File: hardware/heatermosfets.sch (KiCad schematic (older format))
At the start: 39 parts, among them Q1 BUK7M33-60EX, Q2 BUK7M33-60EX, Q3 BUK7M33-60EX, U2 LT1910, U5 OPAMP, U6 LT1910, U7 OPAMP, U8 LT1910, U9 OPAMP

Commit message: Updated Andersons and layout
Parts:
- removed Conn2, Conn5, Conn8: Molex_uF_S_02, MRDT_Connectors:MOLEX_uF_S_02_Horizontal, symbol MRDT_Connectors:Molex_uF_S_02
- removed R10, R12, R13, R14, R15, R2, R3, R4, R5, R7, R8, R9: R, Resistor_SMD:R_0603_1608Metric_Pad0.98x0.95mm_HandSolder, symbol Device:R
- removed U5, U7, U9: OPAMP, Package_SO:SOIC-14_3.9x8.7mm_P1.27mm, symbol pspice:OPAMP
- added Conn3, Conn6, Conn9: Molex_uF_S_03, MRDT_Connectors:MOLEX_uF_S_03_Horizontal, symbol MRDT_Connectors:Molex_uF_S_03
- renumbered C16 to C10, C17 to C11, C18 to C12, C19 to C13, C1 to C8, C2 to C9, Conn9 to Conn10, Conn10 to Conn11, Conn3 to Conn4, Conn4 to Conn5, Conn6 to Conn7, Conn7 to Conn8, R6 to R2, R11 to R3, U2 to U4, U6 to U5, U8 to U6
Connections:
- net +3V3: now also Conn3.1, Conn6.1, Conn9.1
- net GND: now also Conn3.3, Conn6.3, Conn9.3
- net pair1_out: now also Conn3.2
- net pair2_out: now also Conn6.2
- net pair3_out: now also Conn9.2
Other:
- note added: "Temp. Sensor"
- note removed: "Thermistor"

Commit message: Finished layout?
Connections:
- net +12V renamed +12VA
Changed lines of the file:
@@
 Wire Wire Line
 	3200 1550 3200 1700
-$Comp
-L power:+12V #PWR?
-U 1 1 618FC159
-P 2550 1450
-AR Path="/618FC159" Ref="#PWR?"  Part="1"
-AR Path="/618CFEA8/618FC159" Ref="#PWR015"  Part="1"
-F 0 "#PWR015" H 2550 1300 50  0001 C CNN
-F 1 "+12V" H 2565 1623 50  0000 C CNN
-F 2 "" H 2550 1450 50  0001 C CNN
-F 3 "" H 2550 1450 50  0001 C CNN
-	1    2550 1450
-	1    0    0    -1
-$EndComp
 Wire Wire Line
 	2450 1700 3200 1700
@@
 Wire Wire Line
 	6750 1550 6750 1700
-$Comp
-L power:+12V #PWR?
-U 1 1 619075FA
-P 6100 1450
-AR Path="/619075FA" Ref="#PWR?"  Part="1"
-AR Path="/618CFEA8/619075FA" Ref="#PWR020"  Part="1"
-F 0 "#PWR020" H 6100 1300 50  0001 C CNN
-F 1 "+12V" H 6115 1623 50  0000 C CNN
-F 2 "" H 6100 1450 50  0001 C CNN
-F 3 "" H 6100 1450 50  0001 C CNN
-	1    6100 1450
-	1    0    0    -1
-$EndComp
 Wire Wire Line
 	6000 1700 6750 1700
@@
 Wire Wire Line
 	10200 1550 10200 1700
-$Comp
-L power:+12V #PWR?
-U 1 1 61917C2A
-P 9550 1450
-AR Path="/61917C2A" Ref="#PWR?"  Part="1"
-AR Path="/618CFEA8/61917C2A" Ref="#PWR025"  Part="1"
-F 0 "#PWR025" H 9550 1300 50  0001 C CNN
-F 1 "+12V" H 9565 1623 50  0000 C CNN
-F 2 "" H 9550 1450 50  0001 C CNN
-F 3 "" H 9550 1450 50  0001 C CNN
-	1    9550 1450
-	1    0    0    -1
-$EndComp
 Wire Wire Line
 	9450 1700 10200 1700
@@
 Text Notes 10950 3150 0    39   ~ 0
 Temp. Sensor
+$Comp
+L power:+12VA #PWR?
+U 1 1 6190F302
+P 2550 1450
+F 0 "#PWR?" H 2550 1300 50  0001 C CNN
+F 1 "+12VA" H 2565 1623 50  0000 C CNN
+F 2 "" H 2550 1450 50  0001 C CNN
+F 3 "" H 2550 1450 50  0001 C CNN
+	1    2550 1450
+	1    0    0    -1
+$EndComp
+$Comp
+L power:+12VA #PWR?
+U 1 1 61912CB5
+P 6100 1450
+F 0 "#PWR?" H 6100 1300 50  0001 C CNN
+F 1 "+12VA" H 6115 1623 50  0000 C CNN
+F 2 "" H 6100 1450 50  0001 C CNN
+F 3 "" H 6100 1450 50  0001 C CNN
+	1    6100 1450
+	1    0    0    -1
+$EndComp
+$Comp
+L power:+12VA #PWR?
+U 1 1 61913A07
+P 9550 1450
+F 0 "#PWR?" H 9550 1300 50  0001 C CNN
+F 1 "+12VA" H 9565 1623 50  0000 C CNN
+F 2 "" H 9550 1450 50  0001 C CNN
+F 3 "" H 9550 1450 50  0001 C CNN
+	1    9550 1450
+	1    0    0    -1
+$EndComp
 $EndSCHEMATC

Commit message: Fixed rescue library
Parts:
- U4, U5, U6: symbol hardware-rescue:LT1910-MRDT_ICs -> MRDT_ICs:LT1910
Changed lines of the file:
@@
 $EndDescr
 $Comp
-L hardware-rescue:LT1910-MRDT_ICs U?
+L MRDT_ICs:LT1910 U?
 U 1 1 618FC10F
 P 1500 1950
@@
 pair1_in
 $Comp
-L hardware-rescue:LT1910-MRDT_ICs U?
+L MRDT_ICs:LT1910 U?
 U 1 1 619075B4
 P 5050 1950
@@
 pair2_in
 $Comp
-L hardware-rescue:LT1910-MRDT_ICs U?
+L MRDT_ICs:LT1910 U?
 U 1 1 61917BE4
 P 8500 1950

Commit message: Initial Rev2 Design
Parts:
- added D3, D4, D5: LED, LED_SMD:LED_0603_1608Metric_Pad1.05x0.95mm_HandSolder, symbol Device:LED
- added R10, R11, R12: 120, Resistor_SMD:R_0603_1608Metric_Pad0.98x0.95mm_HandSolder, symbol Device:R
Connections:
- net GND: now also D3.1 (K), D4.1 (K), D5.1 (K)
- net pair1_in: now also R10.1
- net pair2_in: now also R11.1
- net pair3_in: now also R12.1
- new net: D5.2 (A), R12.2
- new net: D4.2 (A), R11.2
- new net: D3.2 (A), R10.2
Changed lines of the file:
@@
 	1900 2750 1900 2600
 Wire Wire Line
-	950  1700 1300 1700
+	850  1700 950  1700
 Text Notes 1600 1200 0    59   ~ 12
 Gate Driver
@@
 Wire Wire Line
 	3900 1000 3900 1450
-Text HLabel 950  1700 0    50   Input ~ 0
+Text HLabel 850  1700 0    50   Input ~ 0
 pair1_in
 $Comp
@@
 	5450 2750 5450 2600
 Wire Wire Line
-	4500 1700 4850 1700
+	4400 1700 4500 1700
 Text Notes 5150 1200 0    59   ~ 12
 Gate Driver
@@
 Wire Wire Line
 	7450 1000 7450 1450
-Text HLabel 4500 1700 0    50   Input ~ 0
+Text HLabel 4400 1700 0    50   Input ~ 0
 pair2_in
 $Comp
@@
 	8900 2750 8900 2600
 Wire Wire Line
-	7950 1700 8300 1700
+	7850 1700 7950 1700
 Text Notes 8600 1200 0    59   ~ 12
 Gate Driver
@@
 Wire Wire Line
 	10900 1000 10900 1450
-Text HLabel 7950 1700 0    50   Input ~ 0
+Text HLabel 7850 1700 0    50   Input ~ 0
 pair3_in
 Wire Wire Line
@@
 Temp. Sensor
 $Comp
-L power:+12VA #PWR?
+L power:+12VA #PWR015
 U 1 1 6190F302
 P 2550 1450
-F 0 "#PWR?" H 2550 1300 50  0001 C CNN
+F 0 "#PWR015" H 2550 1300 50  0001 C CNN
 F 1 "+12VA" H 2565 1623 50  0000 C CNN
 F 2 "" H 2550 1450 50  0001 C CNN
@@
 $EndComp
 $Comp
-L power:+12VA #PWR?
+L power:+12VA #PWR020
 U 1 1 61912CB5
 P 6100 1450
-F 0 "#PWR?" H 6100 1300 50  0001 C CNN
+F 0 "#PWR020" H 6100 1300 50  0001 C CNN
 F 1 "+12VA" H 6115 1623 50  0000 C CNN
 F 2 "" H 6100 1450 50  0001 C CNN
@@
 $EndComp
 $Comp
-L power:+12VA #PWR?
+L power:+12VA #PWR025
 U 1 1 61913A07
 P 9550 1450
-F 0 "#PWR?" H 9550 1300 50  0001 C CNN
+F 0 "#PWR025" H 9550 1300 50  0001 C CNN
 F 1 "+12VA" H 9565 1623 50  0000 C CNN
 F 2 "" H 9550 1450 50  0001 C CNN
@@
 	1    0    0    -1
 $EndComp
+Wire Wire Line
+	7950 1700 7950 1850
+Wire Wire Line
+	7950 1850 7800 1850
+Connection ~ 7950 1700
+Wire Wire Line
+	7950 1700 8300 1700
+Wire Wire Line
+	7800 2550 7800 2600
+Wire Wire Line
+	7800 2600 8100 2600
+Connection ~ 8100 2600
+Wire Wire Line
+	4500 1850 4350 1850
+Wire Wire Line
+	4500 1700 4500 1850
+Connection ~ 4500 1700
+Wire Wire Line
+	4500 1700 4850 1700
+Wire Wire Line
+	4350 2550 4350 2600
+Wire Wire Line
+	4350 2600 4650 2600
+Connection ~ 4650 2600
+Wire Wire Line
+	950  1700 950  1850
+Wire Wire Line
+	950  1850 800  1850
+Connection ~ 950  1700
+Wire Wire Line
+	950  1700 1300 1700
+Wire Wire Line
+	800  2550 800  2600
+Wire Wire Line
+	800  2600 1100 2600
+Connection ~ 1100 2600
+$Comp
+L Device:LED D5
+U 1 1 6228CFC5
+P 7800 2400
+F 0 "D5" V 7800 2300 50  0000 R CNN
+F 1 "LED" V 7700 2300 50  0000 R CNN
+F 2 "LED_SMD:LED_0603_1608Metric_Pad1.05x0.95mm_HandSolder" H 7800 2400 50  0001 C CNN
+F 3 "~" H 7800 2400 50  0001 C CNN
+	1    7800 2400
+	0    -1   -1   0
+$EndComp
+$Comp
+L Device:LED D4
+U 1 1 6228DEBB
+P 4350 2400
+F 0 "D4" V 4350 2300 50  0000 R CNN
+F 1 "LED" V 4250 2300 50  0000 R CNN
+F 2 "LED_SMD:LED_0603_1608Metric_Pad1.05x0.95mm_HandSolder" H 4350 2400 50  0001 C CNN
+F 3 "~" H 4350 2400 50  0001 C CNN
+	1    4350 2400
+	0    -1   -1   0
+$EndComp
+$Comp
+L Device:LED D3
+U 1 1 6228F1AF
+P 800 2400
+F 0 "D3" V 800 2300 50  0000 R CNN
+F 1 "LED" V 700 2300 50  0000 R CNN
+F 2 "LED_SMD:LED_0603_1608Metric_Pad1.05x0.95mm_HandSolder" H 800 2400 50  0001 C CNN
+F 3 "~" H 800 2400 50  0001 C CNN
+	1    800  2400
+	0    -1   -1   0
+$EndComp
+Wire Wire Line
+	800  1850 800  1900
+Wire Wire Line
+	4350 1850 4350 1900
+Wire Wire Line
+	7800 1850 7800 1900
+$Comp
+L Device:R R10
+U 1 1 623BB9D6
+P 800 2050
+F 0 "R10" H 870 2096 50  0000 L CNN
+F 1 "120" H 870 2005 50  0000 L CNN
+F 2 "Resistor_SMD:R_0603_1608Metric_Pad0.98x0.95mm_HandSolder" V 730 2050 50  0001 C CNN
+F 3 "~" H 800 2050 50  0001 C CNN
+	1    800  2050
+	1    0    0    -1
+$EndComp
+Wire Wire Line
+	800  2200 800  2250
+$Comp
+L Device:R R11
+U 1 1 623CE605
+P 4350 2050
+F 0 "R11" H 4420 2096 50  0000 L CNN
+F 1 "120" H 4420 2005 50  0000 L CNN
+F 2 "Resistor_SMD:R_0603_1608Metric_Pad0.98x0.95mm_HandSolder" V 4280 2050 50  0001 C CNN
+F 3 "~" H 4350 2050 50  0001 C CNN
+	1    4350 2050
+	1    0    0    -1
+$EndComp
+Wire Wire Line
+	4350 2200 4350 2250
+$Comp
+L Device:R R12
+U 1 1 623D346B
+P 7800 2050
+F 0 "R12" H 7870 2096 50  0000 L CNN
+F 1 "120" H 7870 2005 50  0000 L CNN
+F 2 "Resistor_SMD:R_0603_1608Metric_Pad0.98x0.95mm_HandSolder" V 7730 2050 50  0001 C CNN
+F 3 "~" H 7800 2050 50  0001 C CNN
+	1    7800 2050
+	1    0    0    -1
+$EndComp
+Wire Wire Line
+	7800 2200 7800 2250
 $EndSCHEMATC

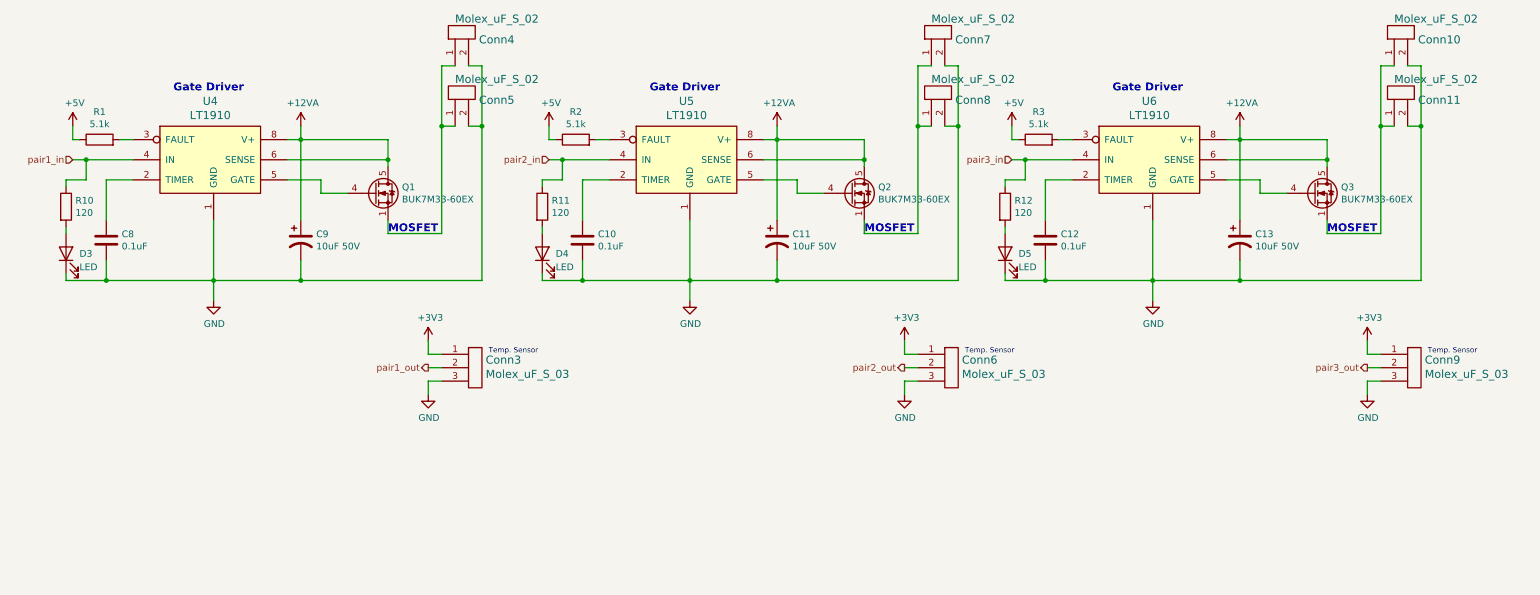
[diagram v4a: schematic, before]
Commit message: Fixed Mosfet LEDs
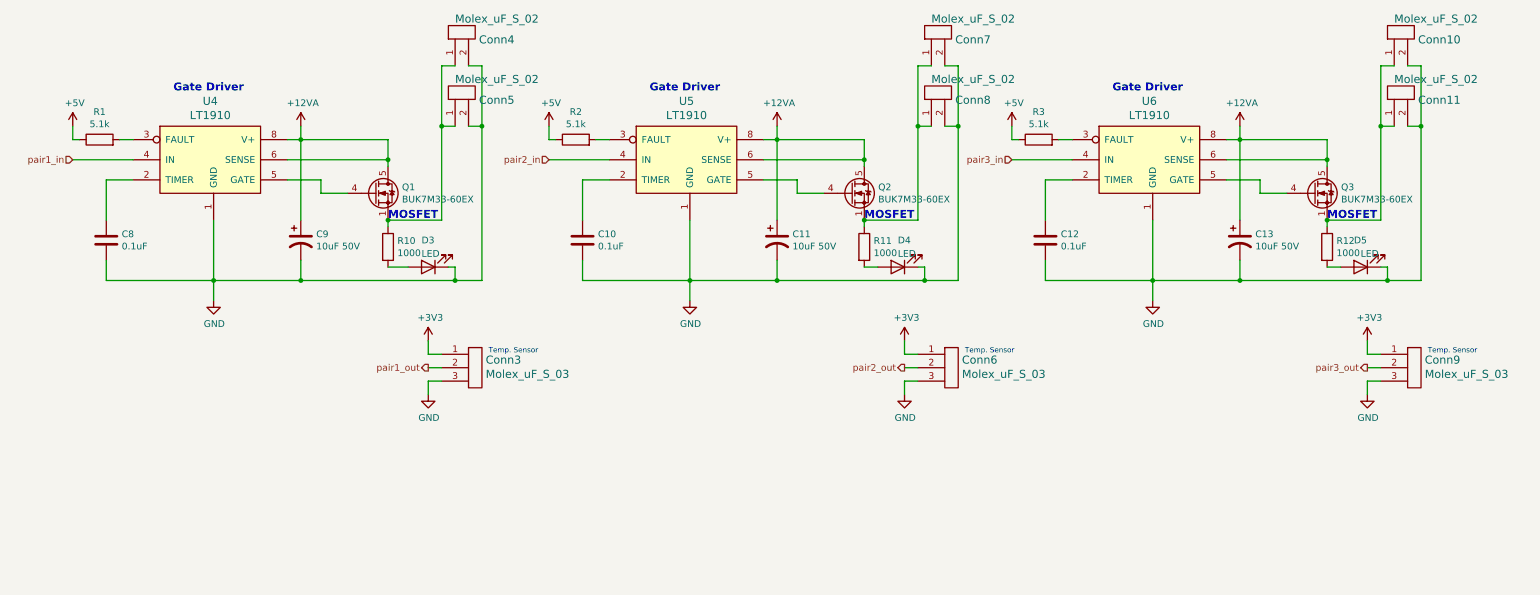
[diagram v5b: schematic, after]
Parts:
- R10, R11, R12: value 120 -> 1000
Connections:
- net pair1_in: no longer R10.1
- net pair2_in: no longer R11.1
- net pair3_in: no longer R12.1
- net at Conn4.1, Conn5.1, Q1.1 (S)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: now also R10.1
- net at Conn7.1, Conn8.1, Q2.1 (S)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: now also R11.1
- net at Conn10.1, Conn11.1, Q3.1 (S)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: now also R12.1
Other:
- moved on the sheet: D3, D4, D5, R10, R11, R12
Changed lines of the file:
@@
 Wire Wire Line
 	1900 2750 1900 2600
-Wire Wire Line
-	850  1700 950  1700
 Text Notes 1600 1200 0    59   ~ 12
 Gate Driver
 Connection ~ 2550 2600
-Text Notes 3200 2250 0    59   ~ 12
+Text Notes 3200 2150 0    59   ~ 12
 MOSFET
 Wire Wire Line
-	3200 2150 3200 2250
-Wire Wire Line
-	3200 2250 3600 2250
-Wire Wire Line
-	3900 2600 2550 2600
+	3200 2150 3600 2150
+Wire Wire Line
+	3900 2600 3700 2600
 Wire Wire Line
 	3200 1550 3200 1700
@@
 Wire Wire Line
 	5450 2750 5450 2600
-Wire Wire Line
-	4400 1700 4500 1700
 Text Notes 5150 1200 0    59   ~ 12
 Gate Driver
 Connection ~ 6100 2600
-Text Notes 6750 2250 0    59   ~ 12
+Text Notes 6750 2150 0    59   ~ 12
 MOSFET
 Wire Wire Line
-	6750 2150 6750 2250
-Wire Wire Line
-	6750 2250 7150 2250
-Wire Wire Line
-	7450 2600 6100 2600
+	6750 2150 7150 2150
+Wire Wire Line
+	7450 2600 7200 2600
 Wire Wire Line
 	6750 1550 6750 1700
@@
 Wire Wire Line
 	8900 2750 8900 2600
-Wire Wire Line
-	7850 1700 7950 1700
 Text Notes 8600 1200 0    59   ~ 12
 Gate Driver
 Connection ~ 9550 2600
-Text Notes 10200 2250 0    59   ~ 12
+Text Notes 10200 2150 0    59   ~ 12
 MOSFET
 Wire Wire Line
-	10200 2150 10200 2250
-Wire Wire Line
-	10200 2250 10600 2250
-Wire Wire Line
-	10900 2600 9550 2600
+	10200 2150 10600 2150
+Wire Wire Line
+	10900 2600 10650 2600
 Wire Wire Line
 	10200 1550 10200 1700
@@
 Connection ~ 3600 1450
 Wire Wire Line
-	3600 1450 3600 2250
+	3600 1450 3600 2150
 Wire Wire Line
 	3800 1450 3900 1450
@@
 Connection ~ 7150 1450
 Wire Wire Line
-	7150 1450 7150 2250
+	7150 1450 7150 2150
 Wire Wire Line
 	7350 1450 7450 1450
@@
 Connection ~ 10600 1450
 Wire Wire Line
-	10600 1450 10600 2250
+	10600 1450 10600 2150
 Wire Wire Line
 	10800 1450 10900 1450
@@
 	1    0    0    -1
 $EndComp
-Wire Wire Line
-	7950 1700 7950 1850
-Wire Wire Line
-	7950 1850 7800 1850
-Connection ~ 7950 1700
-Wire Wire Line
-	7950 1700 8300 1700
-Wire Wire Line
-	7800 2550 7800 2600
-Wire Wire Line
-	7800 2600 8100 2600
-Connection ~ 8100 2600
-Wire Wire Line
-	4500 1850 4350 1850
-Wire Wire Line
-	4500 1700 4500 1850
-Connection ~ 4500 1700
-Wire Wire Line
-	4500 1700 4850 1700
-Wire Wire Line
-	4350 2550 4350 2600
-Wire Wire Line
-	4350 2600 4650 2600
-Connection ~ 4650 2600
-Wire Wire Line
-	950  1700 950  1850
-Wire Wire Line
-	950  1850 800  1850
-Connection ~ 950  1700
-Wire Wire Line
-	950  1700 1300 1700
-Wire Wire Line
-	800  2550 800  2600
-Wire Wire Line
-	800  2600 1100 2600
-Connection ~ 1100 2600
 $Comp
 L Device:LED D5
 U 1 1 6228CFC5
-P 7800 2400
-F 0 "D5" V 7800 2300 50  0000 R CNN
-F 1 "LED" V 7700 2300 50  0000 R CNN
-F 2 "LED_SMD:LED_0603_1608Metric_Pad1.05x0.95mm_HandSolder" H 7800 2400 50  0001 C CNN
-F 3 "~" H 7800 2400 50  0001 C CNN
-	1    7800 2400
-	0    -1   -1   0
+P 10450 2500
+F 0 "D5" H 10500 2300 50  0000 R CNN
+F 1 "LED" H 10450 2400 50  0000 R CNN
+F 2 "LED_SMD:LED_0603_1608Metric_Pad1.05x0.95mm_HandSolder" H 10450 2500 50  0001 C CNN
+F 3 "~" H 10450 2500 50  0001 C CNN
+	1    10450 2500
+	-1   0    0    1
 $EndComp
 $Comp
 L Device:LED D4
 U 1 1 6228DEBB
-P 4350 2400
-F 0 "D4" V 4350 2300 50  0000 R CNN
-F 1 "LED" V 4250 2300 50  0000 R CNN
-F 2 "LED_SMD:LED_0603_1608Metric_Pad1.05x0.95mm_HandSolder" H 4350 2400 50  0001 C CNN
-F 3 "~" H 4350 2400 50  0001 C CNN
-	1    4350 2400
-	0    -1   -1   0
+P 7000 2500
+F 0 "D4" H 7000 2300 50  0000 R CNN
+F 1 "LED" H 7000 2400 50  0000 R CNN
+F 2 "LED_SMD:LED_0603_1608Metric_Pad1.05x0.95mm_HandSolder" H 7000 2500 50  0001 C CNN
+F 3 "~" H 7000 2500 50  0001 C CNN
+	1    7000 2500
+	-1   0    0    1
 $EndComp
 $Comp
 L Device:LED D3
 U 1 1 6228F1AF
-P 800 2400
-F 0 "D3" V 800 2300 50  0000 R CNN
-F 1 "LED" V 700 2300 50  0000 R CNN
-F 2 "LED_SMD:LED_0603_1608Metric_Pad1.05x0.95mm_HandSolder" H 800 2400 50  0001 C CNN
-F 3 "~" H 800 2400 50  0001 C CNN
-	1    800  2400
-	0    -1   -1   0
-$EndComp
-Wire Wire Line
-	800  1850 800  1900
-Wire Wire Line
-	4350 1850 4350 1900
-Wire Wire Line
-	7800 1850 7800 1900
+P 3500 2500
+F 0 "D3" H 3550 2300 50  0000 R CNN
+F 1 "LED" H 3550 2400 50  0000 R CNN
+F 2 "LED_SMD:LED_0603_1608Metric_Pad1.05x0.95mm_HandSolder" H 3500 2500 50  0001 C CNN
+F 3 "~" H 3500 2500 50  0001 C CNN
+	1    3500 2500
+	-1   0    0    1
+$EndComp
 $Comp
 L Device:R R10
 U 1 1 623BB9D6
-P 800 2050
-F 0 "R10" H 870 2096 50  0000 L CNN
-F 1 "120" H 870 2005 50  0000 L CNN
-F 2 "Resistor_SMD:R_0603_1608Metric_Pad0.98x0.95mm_HandSolder" V 730 2050 50  0001 C CNN
-F 3 "~" H 800 2050 50  0001 C CNN
-	1    800  2050
-	1    0    0    -1
-$EndComp
-Wire Wire Line
-	800  2200 800  2250
+P 3200 2350
+F 0 "R10" H 3270 2396 50  0000 L CNN
+F 1 "1000" H 3270 2305 50  0000 L CNN
+F 2 "Resistor_SMD:R_0603_1608Metric_Pad0.98x0.95mm_HandSolder" V 3130 2350 50  0001 C CNN
+F 3 "~" H 3200 2350 50  0001 C CNN
+	1    3200 2350
+	1    0    0    -1
+$EndComp
 $Comp
 L Device:R R11
 U 1 1 623CE605
-P 4350 2050
-F 0 "R11" H 4420 2096 50  0000 L CNN
-F 1 "120" H 4420 2005 50  0000 L CNN
-F 2 "Resistor_SMD:R_0603_1608Metric_Pad0.98x0.95mm_HandSolder" V 4280 2050 50  0001 C CNN
-F 3 "~" H 4350 2050 50  0001 C CNN
-	1    4350 2050
-	1    0    0    -1
-$EndComp
-Wire Wire Line
-	4350 2200 4350 2250
+P 6750 2350
+F 0 "R11" H 6820 2396 50  0000 L CNN
+F 1 "1000" H 6820 2305 50  0000 L CNN
+F 2 "Resistor_SMD:R_0603_1608Metric_Pad0.98x0.95mm_HandSolder" V 6680 2350 50  0001 C CNN
+F 3 "~" H 6750 2350 50  0001 C CNN
+	1    6750 2350
+	1    0    0    -1
+$EndComp
 $Comp
 L Device:R R12
 U 1 1 623D346B
-P 7800 2050
-F 0 "R12" H 7870 2096 50  0000 L CNN
-F 1 "120" H 7870 2005 50  0000 L CNN
-F 2 "Resistor_SMD:R_0603_1608Metric_Pad0.98x0.95mm_HandSolder" V 7730 2050 50  0001 C CNN
-F 3 "~" H 7800 2050 50  0001 C CNN
-	1    7800 2050
-	1    0    0    -1
-$EndComp
-Wire Wire Line
-	7800 2200 7800 2250
+P 10200 2350
+F 0 "R12" H 10270 2396 50  0000 L CNN
+F 1 "1000" H 10270 2305 50  0000 L CNN
+F 2 "Resistor_SMD:R_0603_1608Metric_Pad0.98x0.95mm_HandSolder" V 10130 2350 50  0001 C CNN
+F 3 "~" H 10200 2350 50  0001 C CNN
+	1    10200 2350
+	1    0    0    -1
+$EndComp
+Wire Wire Line
+	850  1700 1300 1700
+Wire Wire Line
+	3200 2150 3200 2200
+Connection ~ 3200 2150
+Wire Wire Line
+	3200 2500 3350 2500
+Wire Wire Line
+	3650 2500 3700 2500
+Wire Wire Line
+	3700 2500 3700 2600
+Connection ~ 3700 2600
+Wire Wire Line
+	3700 2600 2550 2600
+Wire Wire Line
+	6850 2500 6750 2500
+Wire Wire Line
+	7150 2500 7200 2500
+Wire Wire Line
+	7200 2500 7200 2600
+Connection ~ 7200 2600
+Wire Wire Line
+	7200 2600 6100 2600
+Wire Wire Line
+	6750 2200 6750 2150
+Connection ~ 6750 2150
+Wire Wire Line
+	10200 2200 10200 2150
+Connection ~ 10200 2150
+Wire Wire Line
+	10300 2500 10200 2500
+Wire Wire Line
+	10600 2500 10650 2500
+Wire Wire Line
+	10650 2500 10650 2600
+Connection ~ 10650 2600
+Wire Wire Line
+	10650 2600 9550 2600
+Wire Wire Line
+	7850 1700 8300 1700
+Wire Wire Line
+	4400 1700 4850 1700
 $EndSCHEMATC
